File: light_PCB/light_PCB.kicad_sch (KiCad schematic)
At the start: 0 parts

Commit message: all boards routed: light rev B (SOT-23 switches, protected input), pump rev B (CSD18540 MOSFETs), power rev A1 (parts selected), brain Micro-Fit connectors + display on edge; whitelist gitignore
Light, power and pump pass DRC and ERC clean. Brain routed with 0 unconnected; remaining warnings are dangling vias, thin silk text and missing no-connect flags. All cable connectors standardized to Molex Micro-Fit 3.0. Repo now tracks only the KiCad project files, design rules, local libraries and brain 3D models.
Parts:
- added C1: 10uF 50V X7R, Capacitor_SMD:C_1210_3225Metric, symbol Device:C
- added D1: BZT52C8V2, Diode_SMD:D_SOD-123, symbol Device:D_Zener
- added F1: 2A fast, Fuse:Fuse_1206_3216Metric, symbol Device:Fuse
- added J1: NUCLEO CONTROL, Connector_Molex:Molex_Micro-Fit_3.0_43650-0524_1x05-1MP_P3.00mm_Vertical, symbol Connector_Generic:Conn_01x05
- added J2: 12V POWER, Connector_Molex:Molex_Micro-Fit_3.0_43650-0224_1x02-1MP_P3.00mm_Vertical, symbol Connector_Generic:Conn_01x02
- added J3: BLUE OUTPUT, Connector_Molex:Molex_Micro-Fit_3.0_43650-0224_1x02-1MP_P3.00mm_Vertical, symbol Connector_Generic:Conn_01x02
- added J4: RED / NIR OUTPUT, Connector_Molex:Molex_Micro-Fit_3.0_43650-0424_1x04-1MP_P3.00mm_Vertical, symbol Connector_Generic:Conn_01x04
- added J5: WHITE OUTPUT, Connector_Molex:Molex_Micro-Fit_3.0_43650-0224_1x02-1MP_P3.00mm_Vertical, symbol Connector_Generic:Conn_01x02
- added Q1, Q2, Q3, Q4: AO3400A, Package_TO_SOT_SMD:SOT-23, symbol Transistor_FET:AO3400A
- added Q5: AO3401A, Package_TO_SOT_SMD:SOT-23, symbol Transistor_FET:AO3401A
- added R1, R2, R3, R4: 100, HydroLights:R_0402_1005Metric_SilkClearance, symbol Device:R
- added R10: 100k, Resistor_SMD:R_0603_1608Metric, symbol Device:R
- added R5, R6, R7, R8: 10k, HydroLights:R_0402_1005Metric_SilkClearance, symbol Device:R
- added R9: 1k, Resistor_SMD:R_0603_1608Metric, symbol Device:R
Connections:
- new net: Q1.1 (G), R1.2, R5.1
- new net: Q2.1 (G), R2.2, R6.1
- new net: Q3.1 (G), R3.2, R7.1
- new net: Q4.1 (G), R4.2, R8.1
- new net +12V: C1.1, D1.1 (K), J3.2 (Pin_2), J4.1 (Pin_1), J5.2 (Pin_2), Q5.2 (S), R10.1
- new net BLUE_PWM: J1.1 (Pin_1), R1.1
- new net BLUE_SW: J3.1 (Pin_1), Q1.3 (D)
- new net GND: C1.2, J1.5 (Pin_5), J2.2 (Pin_2), Q1.2 (S), Q2.2 (S), Q3.2 (S), Q4.2 (S), R5.2, R6.2, R7.2, R8.2, R9.2
- new net NIR_PWM: J1.2 (Pin_2), R3.1
- new net NIR_SW: J4.3 (Pin_3), Q3.3 (D)
- new net RED_PWM: J1.3 (Pin_3), R2.1
- new net RED_SW: J4.2 (Pin_2), J4.4 (Pin_4), Q2.3 (D)
- new net RP_GATE: D1.2 (A), Q5.1 (G), R10.2, R9.1
- new net VIN_FUSED: F1.2, Q5.3 (D)
- new net VIN_RAW: F1.1, J2.1 (Pin_1)
- new net WHITE_PWM: J1.4 (Pin_4), R4.1
- new net WHITE_SW: J5.1 (Pin_1), Q4.3 (D)
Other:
- note added: "12 V INPUT PROTECTION: F1 then Q5 drain; Q5 source feeds +12V. D1 cathode to source, anode to gate: 8.2 V gate clamp. F1 is replaceable after a fault; verify load/inrush at operating temperature."
- note added: "BLUE"
- note added: "GPIO HIGH = ON; 10k gate pull-down = OFF when disconnected. J4 pins 2/4 = RED; pin 3 = NIR. Common ground to controller. Blue 0.50 A; red + NIR 0.61 A total; white 0.34 A nominal. Q1-Q4: AO3400A, 1=G, 2=S, 3=D. Total load about 1.45 A."
- note added: "NIR"
- note added: "Original Nucleo GPIO mapping: J1.1 BLUE = PE9 J1.2 NIR = PE13 J1.3 RED = PE11 J1.4 WHITE = PB4 J1.5 GND"
- note added: "RED"
- note added: "WHITE"
- title: (none) -> Hydroponic lights - protected 12 V / SMD

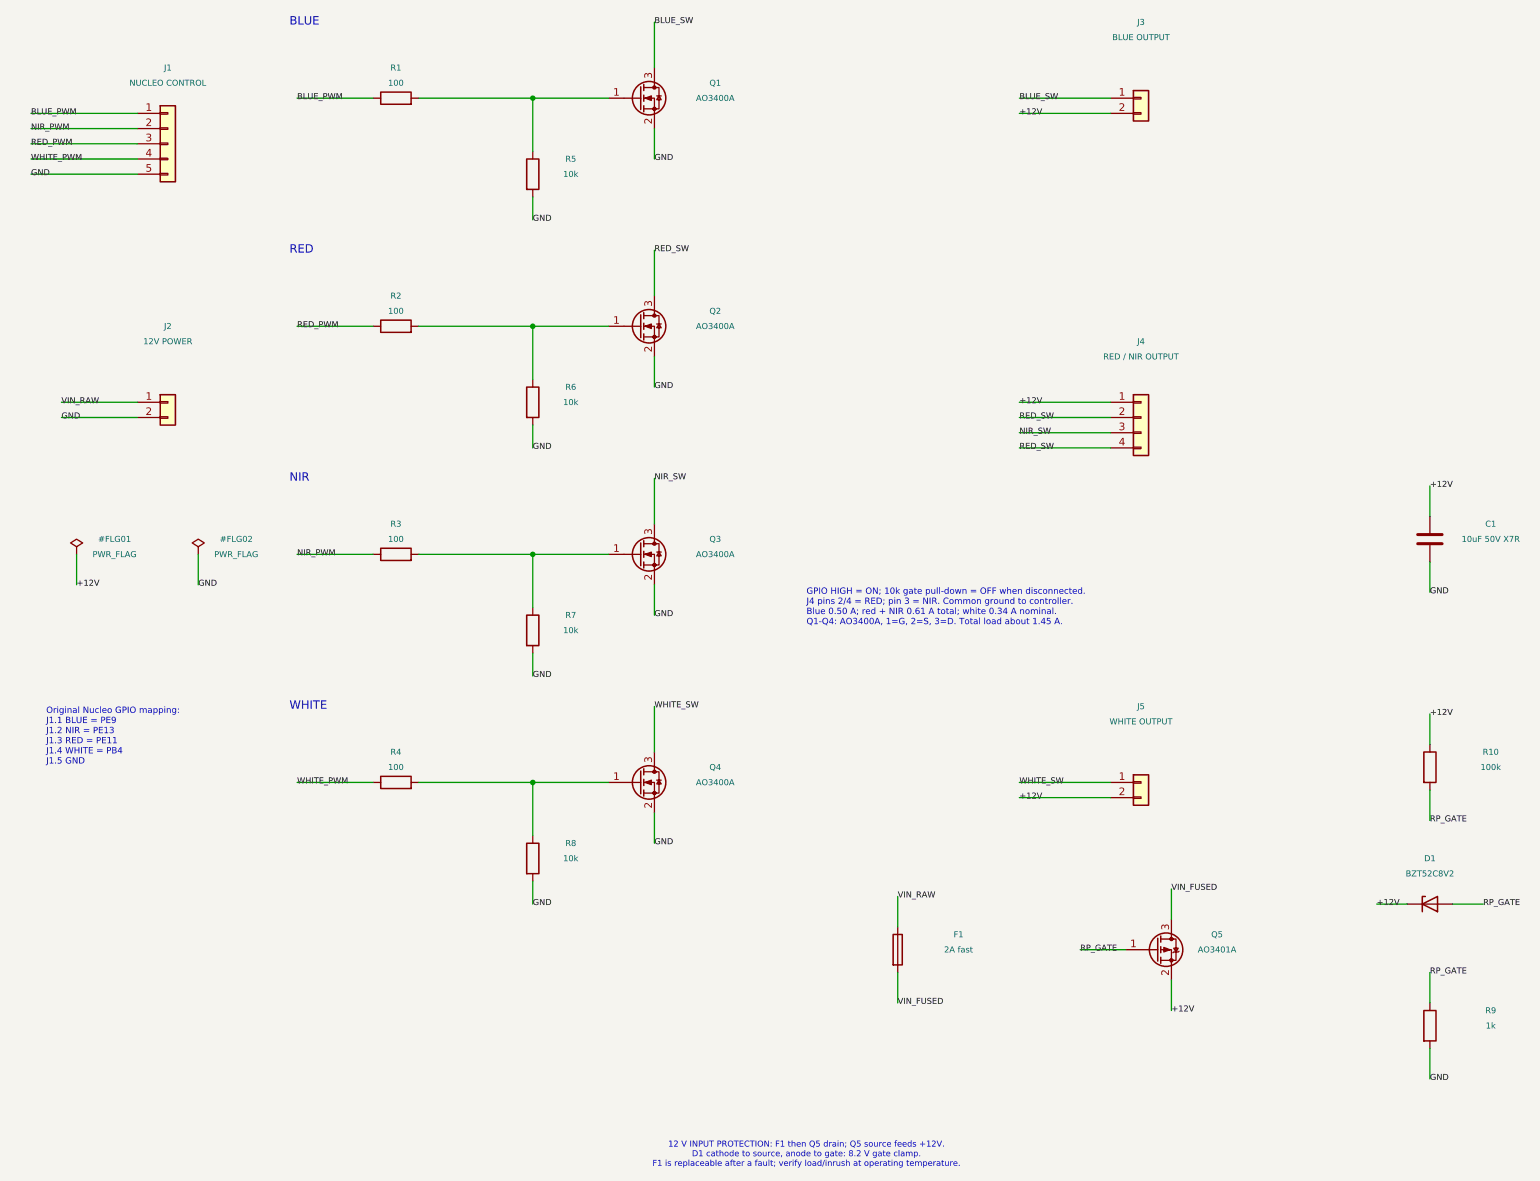
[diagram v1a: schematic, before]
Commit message: Update four KiCad designs and include portable project libraries
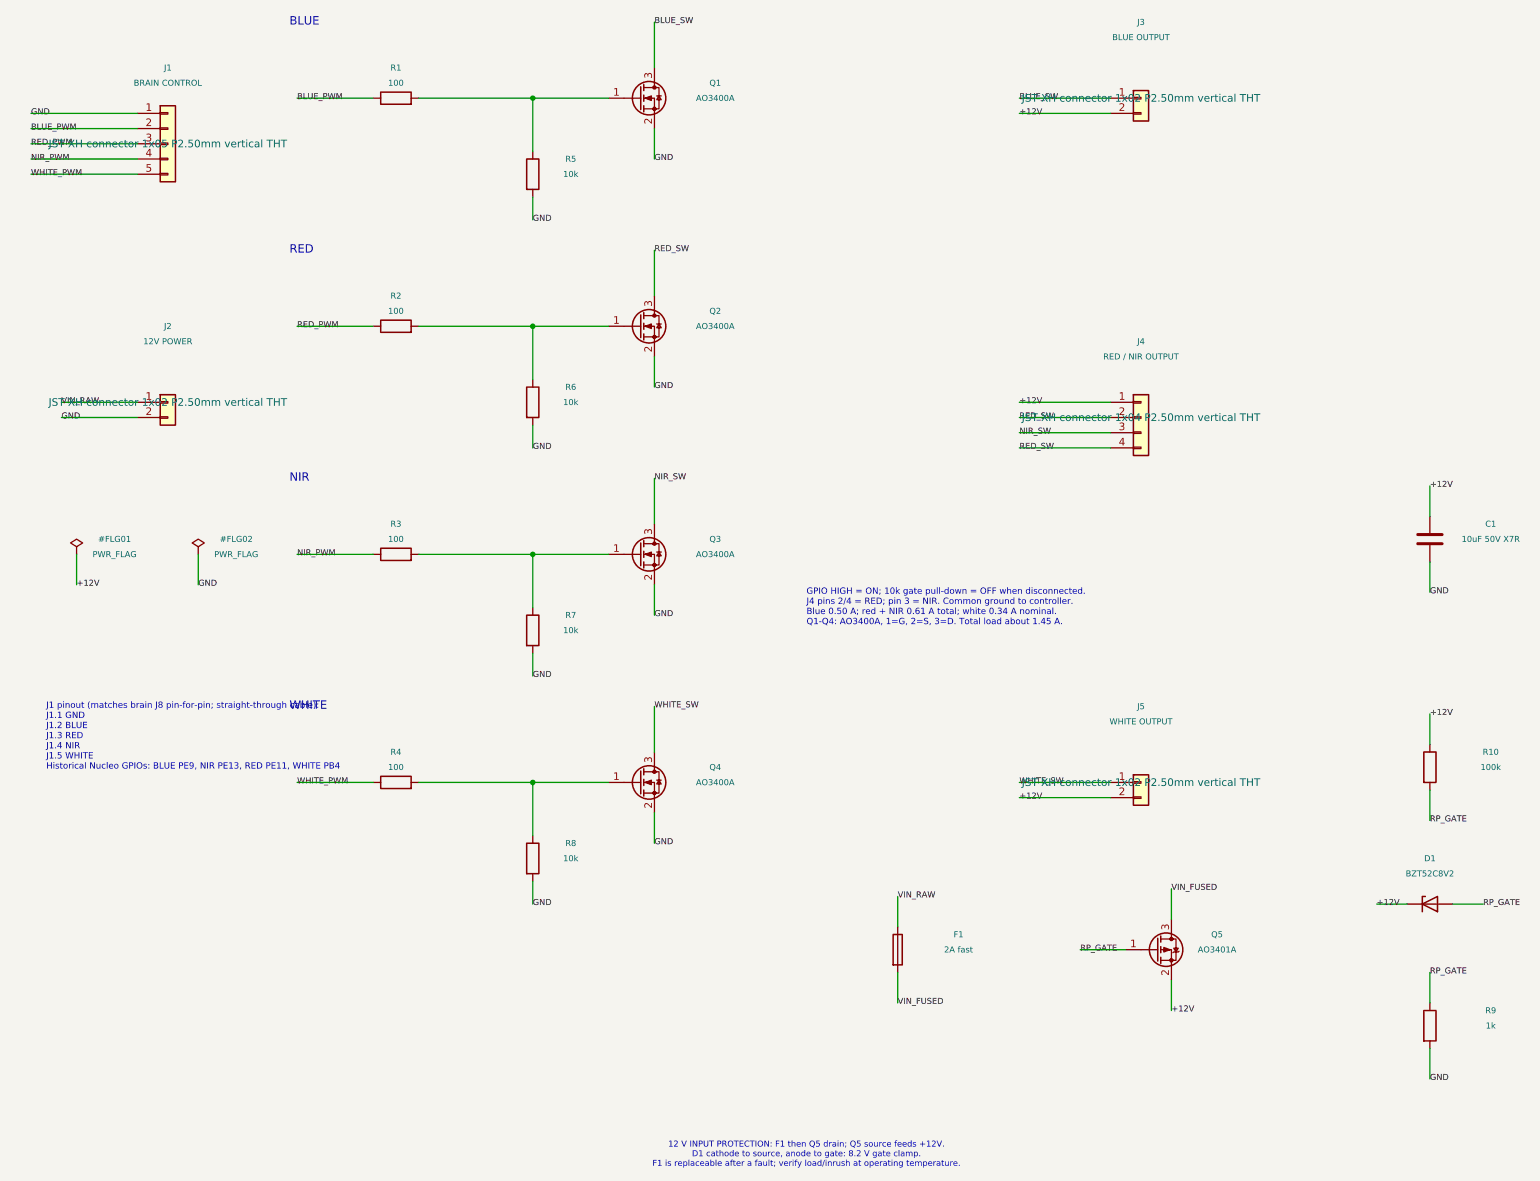
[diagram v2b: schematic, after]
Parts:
- C1: JLCPCB URL (none) -> https://jlcpcb.com/partdetail/MurataElectronics-GRM32ER71H1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; LCSC (none) -> C77102
- D1: Assembly status (none) -> JLC part assigned; check placement and stock at ordering; JLCPCB URL (none) -> https://jlcpcb.com/partdetail/DiodesIncorporated-BZT52C8V2_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; LCSC (none) -> C3001623; MPN BZT52C8V2-7-F -> BZT52C8V2-13-F; Replacement Review (none) -> Same Diodes Incorporated BZT52C8V2 SOD-123, 8.2V; -13-F ree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; Sourcing Status (none) -> Catalog checked for 3 boards of each design; stock not rese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
- F1: Assembly status (none) -> JLC part assigned; check placement and stock at ordering; JLCPCB URL (none) -> https://jlcpcb.com/partdetail/Littelfuse-0466002NRHF/C3105; LCSC (none) -> C3105; MPN 0466002.NR -> 0466002.NRHF; Replacement Review (none) -> Same Littelfuse 466 family, 2A 63V 1206; NRHF halogen-free 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; Sourcing Status (none) -> Catalog checked for 3 boards of each design; stock not rese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
- J1: value NUCLEO CONTROL -> BRAIN CONTROL; footprint Connector_Molex:Molex_Micro-Fit_3.0_43650-0524_1x05-1MP_P3.00mm_Vertical -> Connector_JST:JST_XH_B5B-XH-A_1x05_P2.50mm_Vertical; Assembly status Candidate - verify assembler sourcing and load rating -> JST XH 2.50mm vertical THT, hand-soldered (Taiss XH kit, Am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; MPN 436500524 -> B5B-XH-A(LF)(SN); Manufacturer Molex -> JST (XH-compatible clone OK); Replacement Review (none) -> JST XH 2.50mm vertical THT, hand-soldered (Taiss XH kit, Am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; Selection Notes (none) -> JST XH 2.50mm vertical THT, hand-soldered (Taiss XH kit, Am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; Sourcing Status (none) -> JST XH 2.50mm vertical THT, hand-soldered (Taiss XH kit, Am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
- J2, J3, J5: footprint Connector_Molex:Molex_Micro-Fit_3.0_43650-0224_1x02-1MP_P3.00mm_Vertical -> Connector_JST:JST_XH_B2B-XH-A_1x02_P2.50mm_Vertical; Assembly status Candidate - verify assembler sourcing and load rating -> JST XH 2.50mm vertical THT, hand-soldered (Taiss XH kit, Am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; MPN 436500224 -> B2B-XH-A(LF)(SN); Manufacturer Molex -> JST (XH-compatible clone OK)
- J4: footprint Connector_Molex:Molex_Micro-Fit_3.0_43650-0424_1x04-1MP_P3.00mm_Vertical -> Connector_JST:JST_XH_B4B-XH-A_1x04_P2.50mm_Vertical; Assembly status Candidate - verify assembler sourcing and load rating -> JST XH 2.50mm vertical THT, hand-soldered (Taiss XH kit, Am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; MPN 436500424 -> B4B-XH-A(LF)(SN); Manufacturer Molex -> JST (XH-compatible clone OK)
- Q1, Q2, Q3, Q4: JLCPCB URL (none) -> https://jlcpcb.com/partdetail/Alpha_OmegaSemicon-AO3400A/C2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; LCSC (none) -> C20917
- Q5: JLCPCB URL (none) -> https://jlcpcb.com/partdetail/Alpha_OmegaSemicon-AO3401A/C1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; LCSC (none) -> C15127
- R1, R2, R3, R4: JLCPCB URL (none) -> https://jlcpcb.com/partdetail/YAGEO-RC0402FR07100RL/C106232; LCSC (none) -> C106232
- R10: JLCPCB URL (none) -> https://jlcpcb.com/partdetail/YAGEO-RC0603FR07100KL/C14675; LCSC (none) -> C14675
- R5, R6, R7, R8: JLCPCB URL (none) -> https://jlcpcb.com/partdetail/YAGEO-RC0402FR0710KL/C60490; LCSC (none) -> C60490
- R9: JLCPCB URL (none) -> https://jlcpcb.com/partdetail/YAGEO-RC0603FR071KL/C22548; LCSC (none) -> C22548
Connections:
- net BLUE_PWM: now also J1.2 (Pin_2); no longer J1.1 (Pin_1)
- net GND: now also J1.1 (Pin_1); no longer J1.5 (Pin_5)
- net NIR_PWM: now also J1.4 (Pin_4); no longer J1.2 (Pin_2)
- net WHITE_PWM: now also J1.5 (Pin_5); no longer J1.4 (Pin_4)
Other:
- note added: "J1 pinout (matches brain J8 pin-for-pin; straight-through cable): J1.1 GND J1.2 BLUE J1.3 RED J1.4 NIR J1.5 WHITE Historical Nucleo GPIOs: BLUE PE9, NIR PE13, RED PE11, WHITE PB4"
- note removed: "Original Nucleo GPIO mapping: J1.1 BLUE = PE9 J1.2 NIR = PE13 J1.3 RED = PE11 J1.4 WHITE = PB4 J1.5 GND"
